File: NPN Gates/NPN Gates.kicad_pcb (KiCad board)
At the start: 2 copper layers, 76 x 126 mm, 65 parts, among them J1 Conn_01x02, Q1 BC547, Q10 BC547, Q11 BC547, Q12 BC547, Q13 BC547, Q14 BC547, Q15 BC547, Q16 BC547, Q17 BC547, Q18 BC547, Q19 BC547, Q2 BC547, Q20 BC547, Q21 BC547, Q22 BC547, Q23 BC547, Q24 BC547, Q3 BC547, Q4 BC547, Q5 BC547, Q6 BC547, Q7 BC547, Q8 BC547, Q9 BC547, SW1 A, SW2 B

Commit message: chore: Using D for LEDs instead of DS
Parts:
- renumbered DS1 to D1, DS10 to D10, DS2 to D2, DS3 to D3, DS4 to D4, DS5 to D5, DS6 to D6, DS7 to D7, DS8 to D8, DS9 to D9

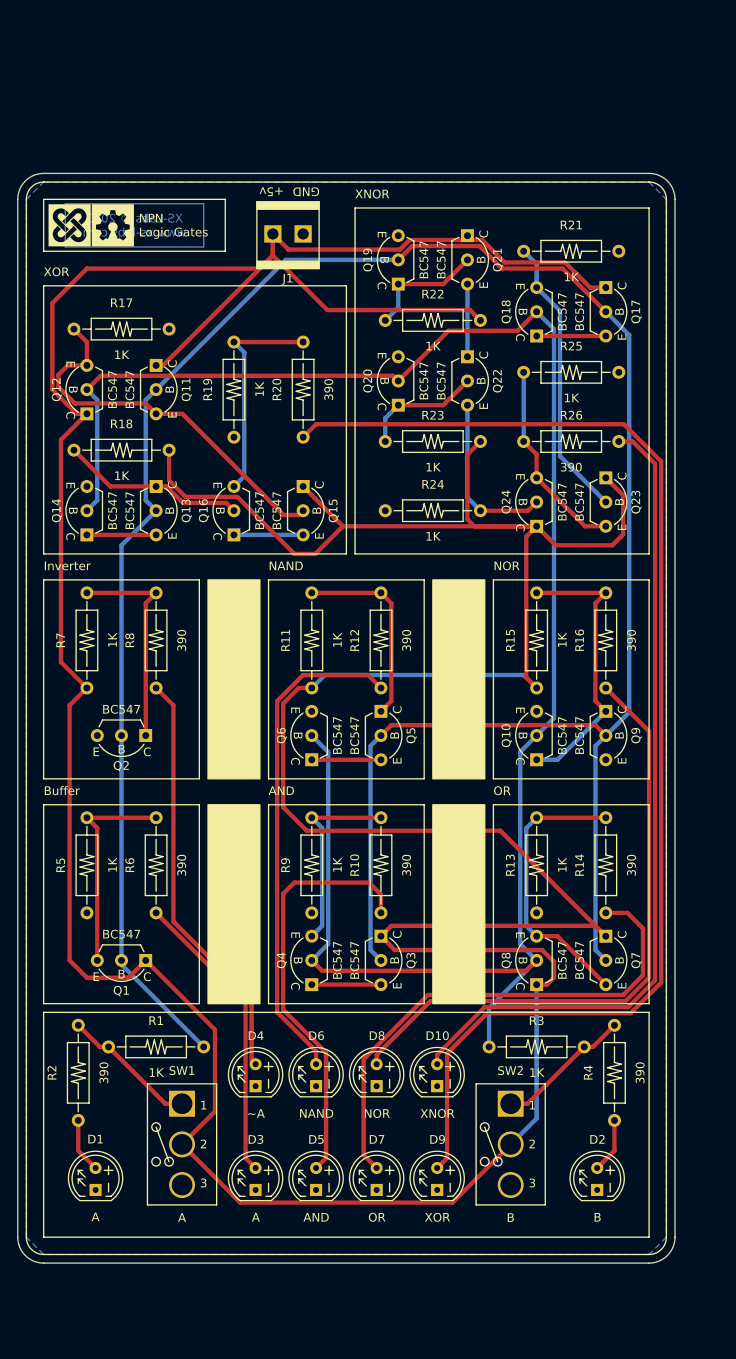
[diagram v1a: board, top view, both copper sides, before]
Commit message: fix: Fixed the NPN Gates project with a new design
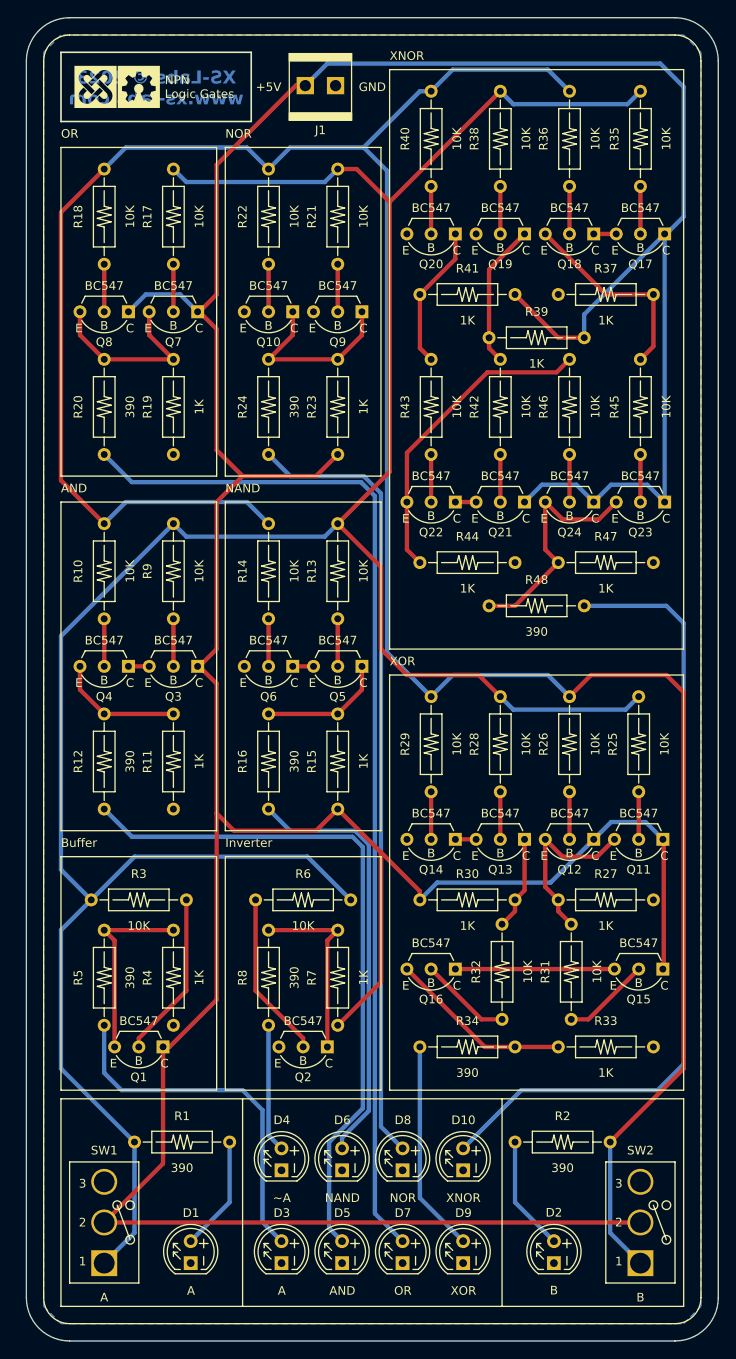
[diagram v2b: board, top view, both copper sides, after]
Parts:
- added R27: 1K, XS:Resistor-Vishay-CCF07, F.Cu at (172.0, 116.0)
- added R28: 10K, XS:Resistor-Vishay-CCF07, F.Cu at (159.8, 98.0)
- added R29: 10K, XS:Resistor-Vishay-CCF07, F.Cu at (151.8, 98.0)
- added R30: 1K, XS:Resistor-Vishay-CCF07, F.Cu at (156.0, 116.0)
- added R31: 10K, XS:Resistor-Vishay-CCF07, F.Cu at (168.0, 124.3)
- added R32: 10K, XS:Resistor-Vishay-CCF07, F.Cu at (160.0, 124.3)
- added R33: 1K, XS:Resistor-Vishay-CCF07, F.Cu at (172.0, 133.0)
- added R34: 390, XS:Resistor-Vishay-CCF07, F.Cu at (156.0, 133.0)
- added R35: 10K, XS:Resistor-Vishay-CCF07, F.Cu at (176.0, 28.0)
- added R36: 10K, XS:Resistor-Vishay-CCF07, F.Cu at (167.8, 28.0)
- added R37: 1K, XS:Resistor-Vishay-CCF07, F.Cu at (172.0, 46.0)
- added R38: 10K, XS:Resistor-Vishay-CCF07, F.Cu at (159.8, 28.0)
- added R39: 1K, XS:Resistor-Vishay-CCF07, F.Cu at (164.0, 51.0)
- added R40: 10K, XS:Resistor-Vishay-CCF07, F.Cu at (151.8, 28.0)
- added R41: 1K, XS:Resistor-Vishay-CCF07, F.Cu at (156.0, 46.0)
- added R42: 10K, XS:Resistor-Vishay-CCF07, F.Cu at (159.8, 59.0)
- added R43: 10K, XS:Resistor-Vishay-CCF07, F.Cu at (151.8, 59.0)
- added R44: 1K, XS:Resistor-Vishay-CCF07, F.Cu at (156.0, 77.0)
- added R45: 10K, XS:Resistor-Vishay-CCF07, F.Cu at (176.0, 59.0)
- added R46: 10K, XS:Resistor-Vishay-CCF07, F.Cu at (167.8, 59.0)
- added R47: 1K, XS:Resistor-Vishay-CCF07, F.Cu at (172.0, 77.0)
- added R48: 390, XS:Resistor-Vishay-CCF07, F.Cu at (164.0, 82.0)
- R1, R24, R5: value 1K -> 390
- R10, R14, R26, R6: value 390 -> 10K
- R13, R17, R18, R21, R22, R25, R3, R9: value 1K -> 10K
- R4: value 390 -> 1K
- moved Q7 90.1 mm to (122.0, 48.0), turned to 0 degrees
- moved Q8 90.1 mm to (114.0, 48.0), turned to 0 degrees
- moved Q11 76.3 mm to (175.8, 109.0), turned to 0 degrees
- moved Q12 76.3 mm to (167.8, 109.0), turned to 0 degrees
- moved Q15 65.7 mm to (175.8, 124.0), turned to 0 degrees
- moved Q10 58.0 mm to (133.0, 48.0), turned to 0 degrees
- moved Q9 58.0 mm to (141.0, 48.0), turned to 0 degrees
- moved Q16 57.7 mm to (151.8, 124.0), turned to 0 degrees
- moved R2 56.6 mm to (167.0, 144.0), turned to 180 degrees
- moved Q13 55.0 mm to (159.8, 109.0), turned to 0 degrees
- moved Q14 55.0 mm to (151.8, 109.0), turned to 0 degrees
- moved R4 52.2 mm to (122.0, 125.0)
- moved R14 51.7 mm to (133.0, 78.0), turned to -90 degrees
- moved R3 49.0 mm to (118.0, 116.0), turned to 0 degrees
- moved R7 48.6 mm to (141.0, 125.0)
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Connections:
- Q1 pad 2: A -> Net-(Q1-B)
- Q10 pad 2: B -> Net-(Q10-B)
- Q11 pad 2: A -> Net-(Q11-B)
- Q12 pad 2: B -> Net-(Q12-B)
- Q13 pad 2: A -> Net-(Q13-B)
- Q14 pad 2: B -> Net-(Q14-B)
- Q15 pad 2: Net-(Q11-E) -> Net-(Q15-B)
- Q16 pad 2: Net-(Q13-C) -> Net-(Q16-B)
- Q17 pad 2: A -> Net-(Q17-B)
- Q18 pad 2: B -> Net-(Q18-B)
- Q19 pad 2: A -> Net-(Q19-B)
- Q2 pad 2: A -> Net-(Q2-B)
- Q20 pad 2: B -> Net-(Q20-B)
- Q21 pad 2: Net-(Q19-C) -> Net-(Q21-B)
- Q22 pad 2: Net-(Q20-C) -> Net-(Q22-B)
- Q23 pad 2: Net-(Q18-E) -> Net-(Q23-B)
- Q24 pad 2: Net-(Q22-E) -> Net-(Q24-B)
- Q3 pad 2: A -> Net-(Q3-B)
- Q4 pad 2: B -> Net-(Q4-B)
- Q5 pad 2: A -> Net-(Q5-B)
- Q6 pad 2: B -> Net-(Q6-B)
- Q7 pad 2: A -> Net-(Q7-B)
- Q8 pad 2: B -> Net-(Q8-B)
- Q9 pad 2: A -> Net-(Q9-B)
- R1 pad 1: Net-(SW1-A) -> A
- R1 pad 2: A -> Net-(D1-A)
- R10 pad 1: Net-(D5-A) -> B
- R10 pad 2: Net-(Q4-E) -> Net-(Q4-B)
- R11 pad 1: VCC -> Net-(Q4-E)
- R11 pad 2: Net-(Q5-C) -> GND
- R12 pad 1: Net-(D6-A) -> Net-(D5-A)
- R12 pad 2: Net-(Q5-C) -> Net-(Q4-E)
- R13 pad 1: Net-(Q7-E) -> A
- R13 pad 2: GND -> Net-(Q5-B)
- R14 pad 1: Net-(D7-A) -> B
- R14 pad 2: Net-(Q7-E) -> Net-(Q6-B)
- R15 pad 2: Net-(Q10-C) -> Net-(Q5-C)
- R16 pad 1: Net-(D8-A) -> Net-(D6-A)
- R16 pad 2: Net-(Q10-C) -> Net-(Q5-C)
- R17 pad 1: Net-(Q11-E) -> A
- R17 pad 2: GND -> Net-(Q7-B)
- R18 pad 1: VCC -> Net-(Q8-B)
- R18 pad 2: Net-(Q13-C) -> B
- R19 pad 1: Net-(Q16-E) -> Net-(Q7-E)
- R2 pad 1: Net-(SW1-A) -> B
- R2 pad 2: Net-(D1-A) -> Net-(D2-A)
- R20 pad 1: Net-(D9-A) -> Net-(D7-A)
- R20 pad 2: Net-(Q16-E) -> Net-(Q7-E)
- R21 pad 1: Net-(Q18-E) -> A
- R21 pad 2: GND -> Net-(Q9-B)
- R22 pad 1: VCC -> Net-(Q10-B)
- R22 pad 2: Net-(Q19-C) -> B
- R23 pad 2: Net-(Q20-C) -> Net-(Q10-C)
- R24 pad 1: Net-(Q22-E) -> Net-(D8-A)
- R24 pad 2: GND -> Net-(Q10-C)
- R25 pad 1: Net-(Q23-E) -> A
- R25 pad 2: GND -> Net-(Q11-B)
- R26 pad 1: Net-(D10-A) -> Net-(Q12-B)
- R26 pad 2: Net-(Q23-E) -> B
- R3 pad 1: Net-(SW2-A) -> A
- R3 pad 2: B -> Net-(Q1-B)
- R4 pad 1: Net-(SW2-A) -> Net-(Q1-E)
- R4 pad 2: Net-(D2-A) -> GND
- R5 pad 1: Net-(Q1-E) -> Net-(D3-A)
- R5 pad 2: GND -> Net-(Q1-E)
- R6 pad 1: Net-(D3-A) -> A
- R6 pad 2: Net-(Q1-E) -> Net-(Q2-B)
- R9 pad 1: Net-(Q4-E) -> A
- R9 pad 2: GND -> Net-(Q3-B)
- SW1 pad 1: Net-(SW1-A) -> A
- SW2 pad 1: Net-(SW2-A) -> B
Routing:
- net Net-(D9-A): track 145.9 -> 24.5 mm
- net VCC: track 555.6 -> 472.6 mm
- net B: track 216.3 -> 298.7 mm
- net Net-(D7-A): track 60.0 -> 120.8 mm
- net Net-(D4-A): track 48.3 -> 14.9 mm
- net Net-(D5-A): track 48.8 -> 79.5 mm
- net A: track 276.8 -> 306.1 mm
- net Net-(Q11-E): track 44.6 -> 20.7 mm
- net Net-(D8-A): track 71.8 -> 91.6 mm
- net Net-(Q2-B): track 0.00 -> 19.3 mm
- net Net-(Q1-B): track 0.00 -> 19.3 mm
- net Net-(Q22-E): track 19.7 -> 36.6 mm
- net Net-(SW2-A): track 15.8 -> 0.00 mm
- net Net-(SW1-A): track 15.8 -> 0.00 mm
- net Net-(Q7-E): track 33.0 -> 21.3 mm
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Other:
- board size 76 x 126 mm -> 80 x 153 mm
- board text added: "+5V"
- board text removed: "+5v"
